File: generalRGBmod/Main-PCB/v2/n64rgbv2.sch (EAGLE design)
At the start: 77 parts, among them J3 2510-, U1 5M570ZT100C5, U2 ADV7125/ADV7123, U4 TLV70018-DDC

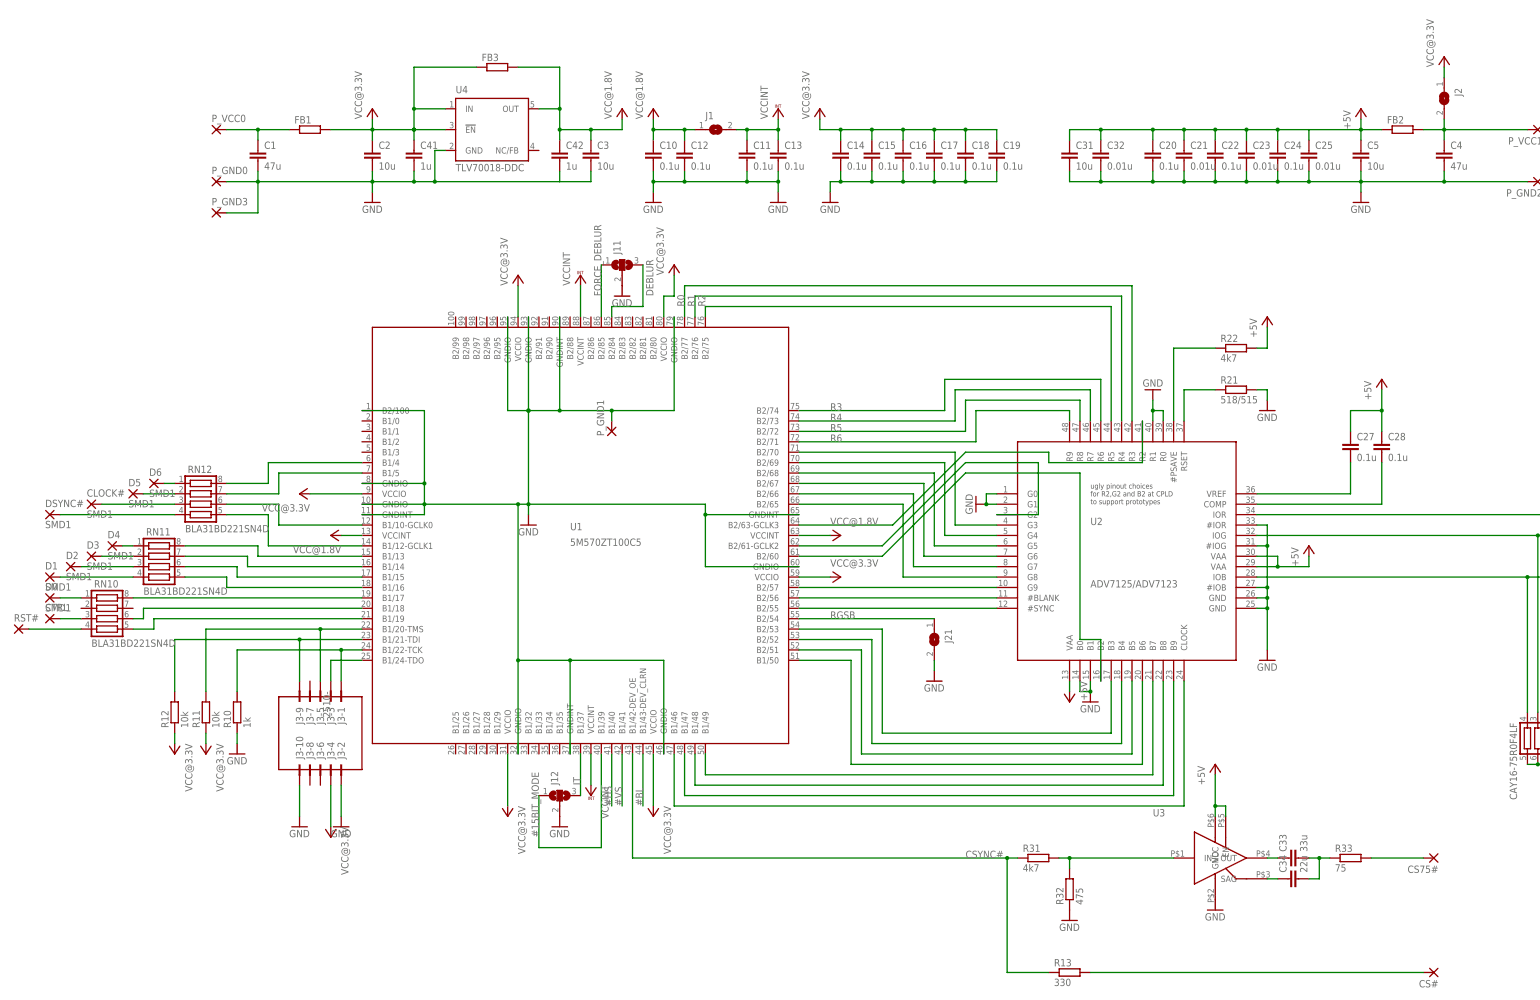
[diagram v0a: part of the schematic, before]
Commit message: PCB Update: remove jumper for analog power supply I recommend 5V for the analog part anyway. So now the user is forced to use 5V here!
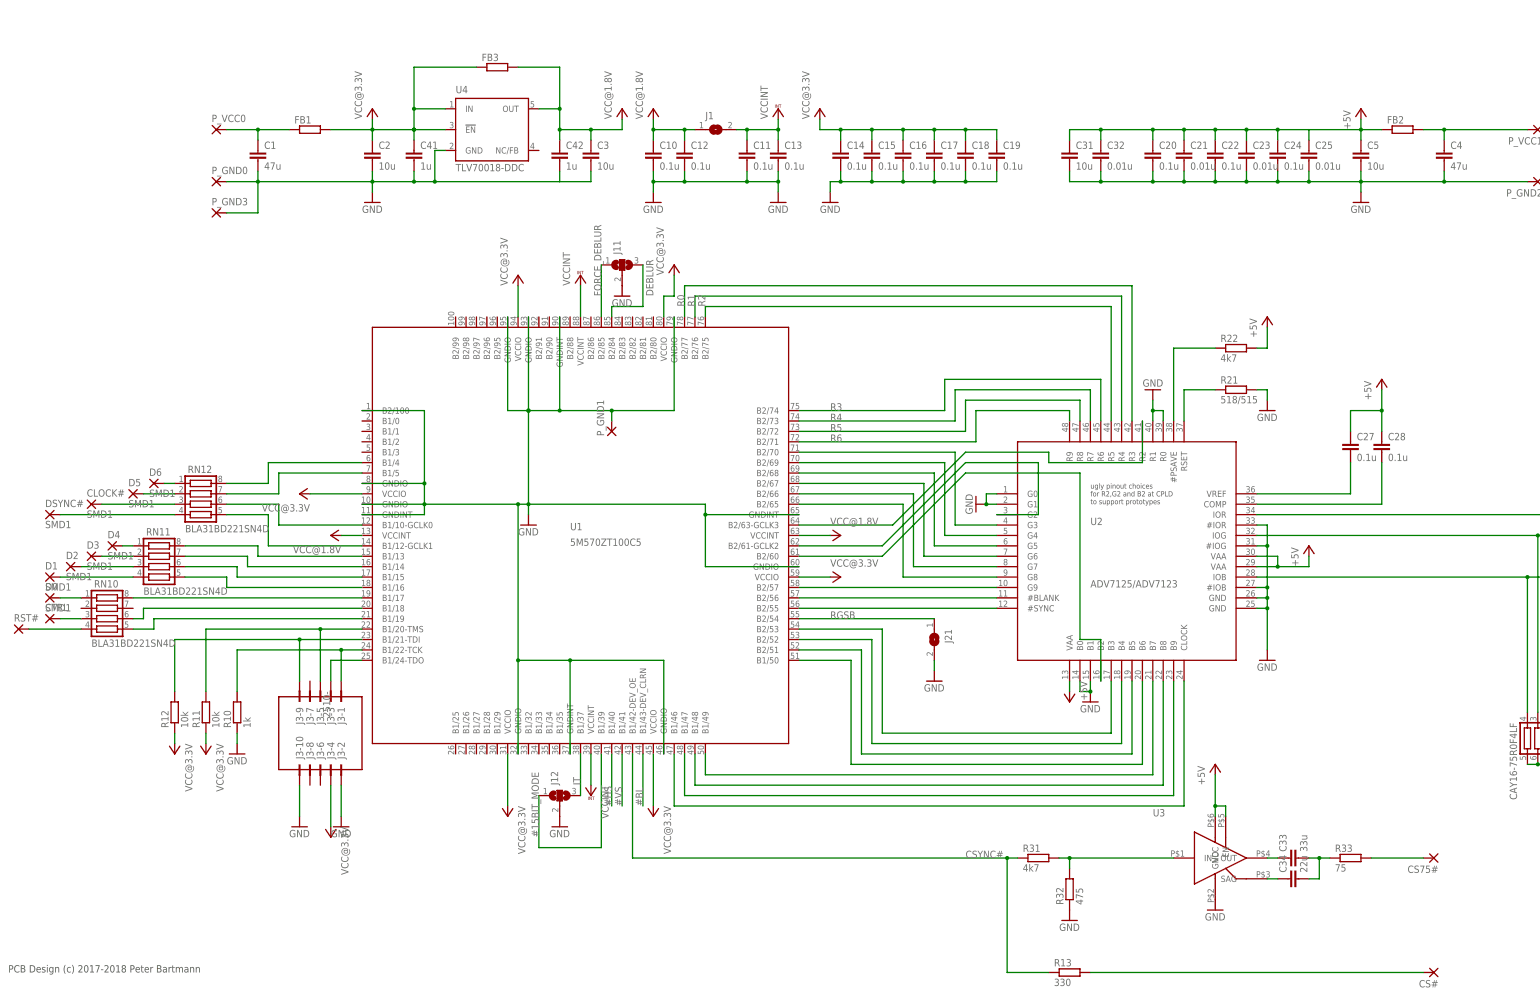
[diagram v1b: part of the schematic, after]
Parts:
- removed J2: (no value), jumper:SJ
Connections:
- net N$44: no longer J2.2
- net VCC@3.3V: no longer J2.1
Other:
- note added: "PCB Design (c) 2017-2018 Peter Bartmann"
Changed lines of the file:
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@@
 <?xml version="1.0" encoding="utf-8"?>
 <!DOCTYPE eagle SYSTEM "eagle.dtd">
-<eagle version="8.5.0">
+<eagle version="8.6.0">
 <drawing>
 <settings>
@@
 <part name="C5" library="rcl" deviceset="C-EU" device="C0805" value="10u"/>
 <part name="P+1" library="supply1" library_urn="urn:adsk.eagle:library:371" deviceset="+5V" device=""/>
-<part name="J2" library="jumper" deviceset="SJ" device=""/>
-<part name="P+23" library="supply1" library_urn="urn:adsk.eagle:library:371" deviceset="VCC" device="" value="VCC@3.3V"/>
 <part name="C25" library="rcl" deviceset="C-EU" device="C0603" value="0.01u"/>
 <part name="C24" library="rcl" deviceset="C-EU" device="C0603" value="0.1u"/>
@@
 for R2,G2 and B2 at CPLD
 to support prototypes</text>
+<text x="5.08" y="15.24" size="1.778" layer="97" font="vector">PCB Design (c) 2017-2018 Peter Bartmann</text>
 </plain>
 <instances>
@@
 <instance part="C5" gate="G$1" x="335.28" y="215.9"/>
 <instance part="P+1" gate="1" x="335.28" y="226.06"/>
-<instance part="J2" gate="1" x="355.6" y="228.6" rot="R270"/>
-<instance part="P+23" gate="VCC" x="355.6" y="238.76"/>
 <instance part="C25" gate="G$1" x="322.58" y="215.9"/>
 <instance part="C24" gate="G$1" x="314.96" y="215.9"/>
@@
 <wire x1="45.72" y1="71.12" x2="45.72" y2="73.66" width="0.1524" layer="91"/>
 </segment>
-<segment>
-<pinref part="J2" gate="1" pin="1"/>
-<pinref part="P+23" gate="VCC" pin="VCC"/>
-<wire x1="355.6" y1="233.68" x2="355.6" y2="236.22" width="0.1524" layer="91"/>
-</segment>
 </net>
 <net name="N$13" class="0">
@@
 <wire x1="355.6" y1="218.44" x2="355.6" y2="220.98" width="0.1524" layer="91"/>
 <junction x="355.6" y="220.98"/>
-<pinref part="J2" gate="1" pin="2"/>
-<wire x1="355.6" y1="220.98" x2="355.6" y2="223.52" width="0.1524" layer="91"/>
-</segment>
-</net>
+</segment>
+</net>

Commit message: pcb update: add some additional pads for rst and ctrl io
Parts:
- added CTRL_A, RST#_A: SMD1, wirepad:SMD1
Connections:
- net N$5: now also RST#_A.P
- net N$6: now also CTRL_A.P
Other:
- note added: "PCB Design (c) 2017-2019 Peter Bartmann"
- note removed: "PCB Design (c) 2017-2018 Peter Bartmann"
- moved on the sheet: CTRL, D0, RST#
